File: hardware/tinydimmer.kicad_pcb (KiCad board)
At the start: 2 copper layers, 34 parts, among them J1 CTB7000/6, J2 CTB7000/2, Q1 IRL540N, SW1 SW_Push, T1 Hahn EL 305 2051, U1 BAJ0CC0T, U2 Digispark USB

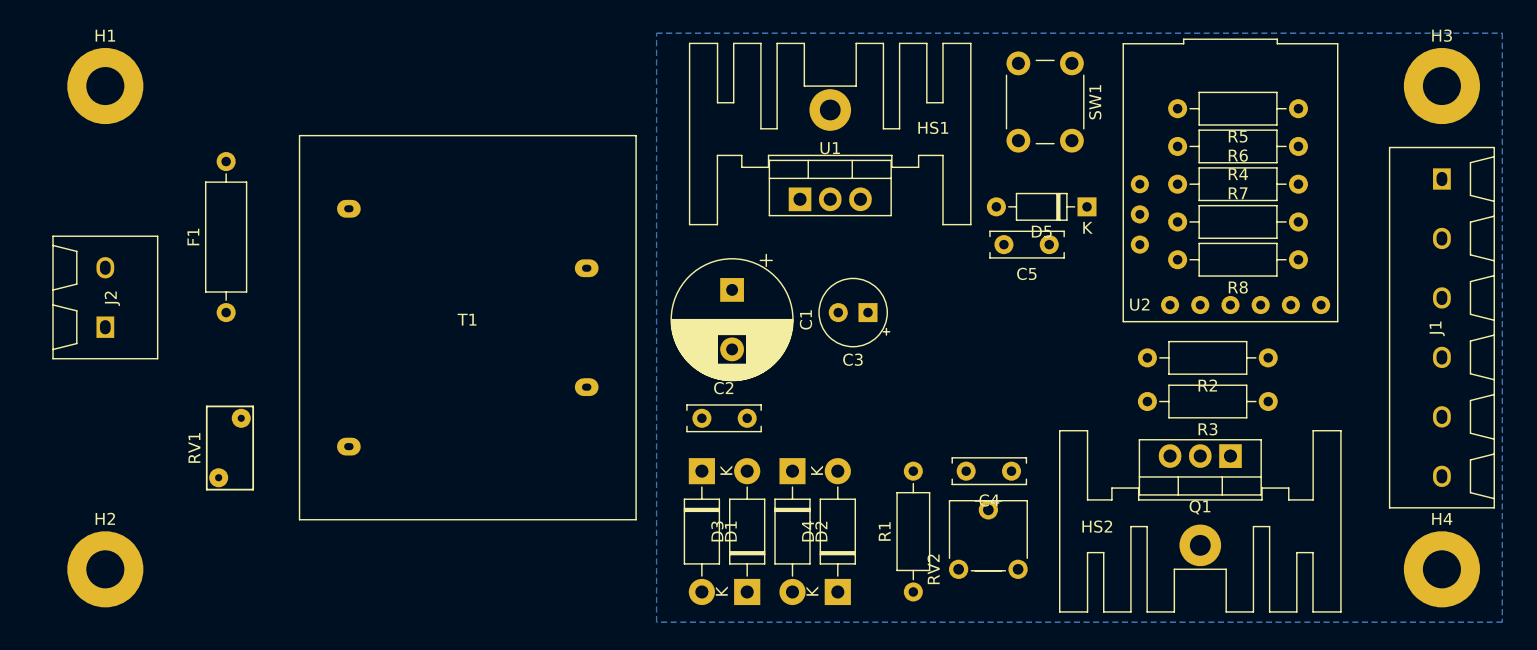
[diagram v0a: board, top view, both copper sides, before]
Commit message: Adjust pads, rewire connectors, change footprints
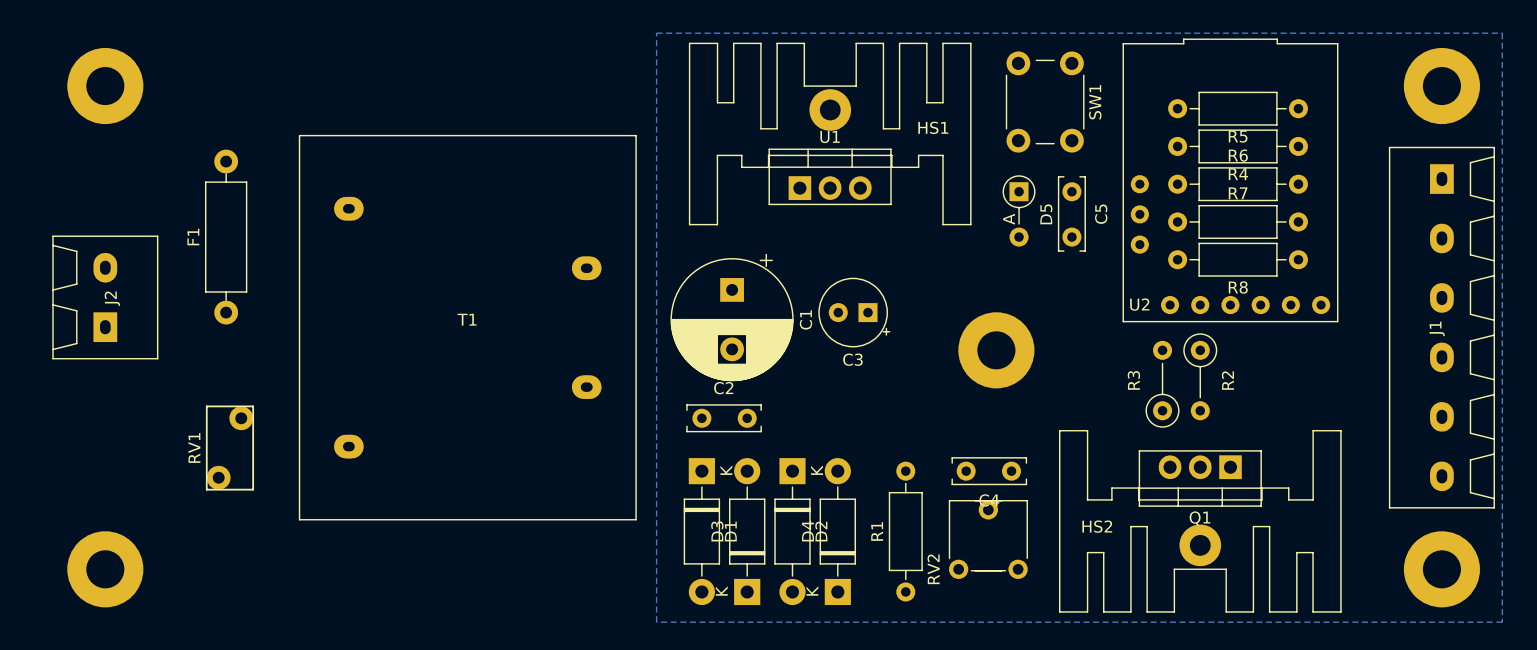
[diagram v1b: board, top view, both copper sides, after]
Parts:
- added H5: MountingHole_Pad, MountingHole:MountingHole_3.2mm_M3_Pad, F.Cu at (112.4, 65.4)
- D5: footprint Diode_THT:D_DO-35_SOD27_P7.62mm_Horizontal -> Diode_THT:D_DO-35_SOD27_P3.81mm_Vertical_AnodeUp
- R2, R3: footprint Resistor_THT:R_Axial_DIN0207_L6.3mm_D2.5mm_P10.16mm_Horizontal -> Resistor_THT:R_Axial_DIN0207_L6.3mm_D2.5mm_P5.08mm_Vertical
- moved R3 8.92 mm to (126.4, 70.5), turned to 90 degrees
- moved D5 5.85 mm to (114.3, 52.1), turned to 270 degrees
- moved R2 5.75 mm to (129.5, 65.4), turned to 270 degrees
- moved C5 5.24 mm to (118.7, 51.4), turned to 270 degrees
- moved U1 0.94 mm to (95.9, 51.8)
- moved Q1 0.94 mm to (132.1, 75.2)
- moved R1 0.63 mm to (104.8, 85.7)
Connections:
- J1 pad 1: SW_NEG -> SW_POS
- J1 pad 3: SW_POS -> GND
- J1 pad 5: GND -> SW_NEG
- R2 pad 1: Net-(Q1-Pad1) -> PWM
- R2 pad 2: PWM -> Net-(Q1-Pad1)

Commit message: First PCB draft
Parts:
- D5: footprint Diode_THT:D_DO-35_SOD27_P3.81mm_Vertical_AnodeUp -> Diode_THT:D_DO-35_SOD27_P7.62mm_Horizontal
- moved D5 17.1 mm to (128.3, 42.2), turned to 0 degrees
- moved C5 6.86 mm to (119.0, 58.3), turned to 180 degrees
- moved H3 1.00 mm to (148.9, 43.2)
- moved H4 1.00 mm to (148.9, 83.8)
- moved J1 1.00 mm to (148.9, 63.5)
- moved RV1 0.32 mm to (48.6, 71.1)
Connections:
- C5 pad 1: Net-(C5-Pad1) -> ENABLE
- D5 pad 1: Net-(C5-Pad1) -> Net-(D5-Pad1)
- R6 pad 1: Net-(C5-Pad1) -> Net-(D5-Pad1)
- R7 pad 2: Net-(C5-Pad1) -> Net-(D5-Pad1)
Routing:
- net POT_POS: track 0.00 -> 51.3 mm
- net +10V: track 0.00 -> 50.0 mm
- net Net-(D2-Pad2): track 0.00 -> 40.9 mm
- net Net-(C1-Pad1): track 0.00 -> 38.2 mm
- net SENSE: track 0.00 -> 31.2 mm
- net NEUT: track 0.00 -> 30.0 mm
- net Net-(R4-Pad1): track 0.00 -> 28.0 mm
- net Net-(D1-Pad2): track 0.00 -> 25.0 mm
- net Net-(F1-Pad1): track 0.00 -> 24.0 mm
- net Net-(D5-Pad1): track 0.00 -> 22.4 mm
- net RESET: track 0.00 -> 17.9 mm
- net ENABLE: track 0.00 -> 17.3 mm
- net LINE: track 0.00 -> 15.2 mm
- net SW_POS: track 0.00 -> 11.2 mm
- net Net-(Q1-Pad1): track 0.00 -> 9.64 mm
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- added copper zone on F.Cu, net SW_NEG
- added copper zone on B.Cu, net SW_POS
- added copper zone on F.Cu, net SW_POS
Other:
- board outline added: 125.2 x 50.2 mm
- net class Default: clearance 0.2 -> 0.25; trace_width 0.25 -> 0.5
- net class Mains added: clearance 1, trace_width 1.5, via_dia 0.8, via_drill 0.4
- net class Power added: clearance 0.5, trace_width 1.5, via_dia 0.8, via_drill 0.4
- rule trace_clearance: 0.2 -> 0.25
- board text added: "L"
- board text added: "LED+"
- board text added: "LED-"
- board text added: "N"
- board text added: "POT+"
- board text added: "POT-"
- board text added: "PSU+"
- board text added: "PSU-"

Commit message: Make labels more visible
Gerbers for first production batch
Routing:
- net SENSE: track 31.2 -> 31.8 mm
- net SW_POS: vias 0 -> 16
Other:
- board text added: "2A max"
- board text added: "RESET"

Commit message: Replace plain MOV with a protected GMOV
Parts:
- RV1: value 7N431K -> 14D271K; footprint Varistor:RV_Disc_D7mm_W3.9mm_P5mm -> Varistor:RV_Disc_D15.5mm_W3.9mm_P7.5mm
- moved F1 3.08 mm to (47.4, 59.2)
- moved RV1 1.31 mm to (48.4, 69.8)
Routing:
- net LINE: track 15.2 -> 17.6 mm
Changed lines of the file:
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@@
     (thickness 1.6)
     (drawings 18)
-    (tracks 108)
+    (tracks 104)
     (zones 0)
     (modules 35)
@@
     (add_net SW_NEG)
     (add_net SW_POS)
+  )
+  (module Varistor:RV_Disc_D15.5mm_W3.9mm_P7.5mm (layer F.Cu)
+    (at 48.4124 69.8246 270)
+    (descr "Varistor, diameter 15.5mm, width 3.9mm, pitch 7.5mm")
+    (tags "varistor SIOV")
+    (fp_text reference RV1 (at 3.75 3.65 90) (layer F.SilkS)
+      (effects (font (size 1 1) (thickness 0.15)))
+    )
+    (fp_text value 14D271K (at 3.75 -2.25 90) (layer F.Fab)
+      (effects (font (size 1 1) (thickness 0.15)))
+    )
+    (fp_line (start -4 -1.25) (end -4 2.65) (layer F.Fab) (width 0.1))
+    (fp_line (start 11.5 -1.25) (end 11.5 2.65) (layer F.Fab) (width 0.1))
+    (fp_line (start -4 -1.25) (end 11.5 -1.25) (layer F.Fab) (width 0.1))
+    (fp_line (start -4 2.65) (end 11.5 2.65) (layer F.Fab) (width 0.1))
+    (fp_line (start -4 -1.25) (end -4 2.65) (layer F.SilkS) (width 0.15))
+    (fp_line (start 11.5 -1.25) (end 11.5 2.65) (layer F.SilkS) (width 0.15))
+    (fp_line (start -4 -1.25) (end 11.5 -1.25) (layer F.SilkS) (width 0.15))
+    (fp_line (start -4 2.65) (end 11.5 2.65) (layer F.SilkS) (width 0.15))
+    (fp_line (start -4.25 -1.5) (end -4.25 2.9) (layer F.CrtYd) (width 0.05))
+    (fp_line (start 11.75 -1.5) (end 11.75 2.9) (layer F.CrtYd) (width 0.05))
+    (fp_line (start -4.25 -1.5) (end 11.75 -1.5) (layer F.CrtYd) (width 0.05))
+    (fp_line (start -4.25 2.9) (end 11.75 2.9) (layer F.CrtYd) (width 0.05))
+    (fp_text user %R (at 3.75 0.7 90) (layer F.Fab)
+      (effects (font (size 1 1) (thickness 0.15)))
+    )
+    (pad 2 thru_hole circle (at 7.5 1.4 270) (size 1.8 1.8) (drill 0.8) (layers *.Cu *.Mask)
+      (net 12 NEUT))
+    (pad 1 thru_hole circle (at 0 0 270) (size 1.8 1.8) (drill 0.8) (layers *.Cu *.Mask)
+      (net 7 "Net-(F1-Pad1)"))
+    (model ${KISYS3DMOD}/Varistor.3dshapes/RV_Disc_D15.5mm_W3.9mm_P7.5mm.wrl
+      (at (xyz 0 0 0))
+      (scale (xyz 1 1 1))
+      (rotate (xyz 0 0 0))
+    )
   )
   (module Diode_THT:D_DO-35_SOD27_P7.62mm_Horizontal (layer F.Cu)
@@
   )
   (module Resistor_THT:R_Axial_DIN0309_L9.0mm_D3.2mm_P12.70mm_Horizontal (layer F.Cu)
-    (at 47.625 62.23 90)
+    (at 47.3964 59.1566 90)
     (descr "Resistor, Axial_DIN0309 series, Axial, Horizontal, pin pitch=12.7mm, 0.5W = 1/2W, length*diameter=9*3.2mm^2, http://cdn-reichelt.de/documents/datenblatt/B400/1_4W%23YAG.pdf")
     (tags "Resistor Axial_DIN0309 series Axial Horizontal pin pitch 12.7mm 0.5W = 1/2W length 9mm diameter 3.2mm")
@@
     )
   )
-  (module Varistor:RV_Disc_D7mm_W3.9mm_P5mm (layer F.Cu)
-    (at 48.5775 71.12 270)
-    (descr "Varistor, diameter 7mm, width 3.9mm, pitch 5mm")
-    (tags "varistor SIOV")
-    (fp_text reference RV1 (at -2.3622 2.0447 180) (layer F.SilkS)
-      (effects (font (size 1 1) (thickness 0.15)))
-    )
-    (fp_text value 7N431K (at 2.5 -2 90) (layer F.Fab)
-      (effects (font (size 1 1) (thickness 0.15)))
-    )
-    (fp_text user %R (at 2.5 0.95 90) (layer F.Fab)
-      (effects (font (size 1 1) (thickness 0.15)))
-    )
-    (fp_line (start -1.25 3.15) (end 6.25 3.15) (layer F.CrtYd) (width 0.05))
-    (fp_line (start -1.25 -1.25) (end 6.25 -1.25) (layer F.CrtYd) (width 0.05))
-    (fp_line (start 6.25 -1.25) (end 6.25 3.15) (layer F.CrtYd) (width 0.05))
-    (fp_line (start -1.25 -1.25) (end -1.25 3.15) (layer F.CrtYd) (width 0.05))
-    (fp_line (start -1 2.9) (end 6 2.9) (layer F.SilkS) (width 0.15))
-    (fp_line (start -1 -1) (end 6 -1) (layer F.SilkS) (width 0.15))
-    (fp_line (start 6 -1) (end 6 2.9) (layer F.SilkS) (width 0.15))
-    (fp_line (start -1 -1) (end -1 2.9) (layer F.SilkS) (width 0.15))
-    (fp_line (start -1 2.9) (end 6 2.9) (layer F.Fab) (width 0.1))
-    (fp_line (start -1 -1) (end 6 -1) (layer F.Fab) (width 0.1))
-    (fp_line (start 6 -1) (end 6 2.9) (layer F.Fab) (width 0.1))
-    (fp_line (start -1 -1) (end -1 2.9) (layer F.Fab) (width 0.1))
-    (pad 1 thru_hole circle (at 0 0 270) (size 2 2) (drill 0.8) (layers *.Cu *.Mask)
-      (net 7 "Net-(F1-Pad1)"))
-    (pad 2 thru_hole circle (at 5 1.9 270) (size 2 2) (drill 0.8) (layers *.Cu *.Mask)
-      (net 12 NEUT))
-    (model ${KISYS3DMOD}/Varistor.3dshapes/RV_Disc_D7mm_W3.9mm_P5mm.wrl
-      (at (xyz 0 0 0))
-      (scale (xyz 1 1 1))
-      (rotate (xyz 0 0 0))
-    )
-  )
   (module custom-parts:Potentiometer_ACP_CA6-V2,5_Vertical (layer F.Cu)
     (at 109.22 83.82 90)
@@
       (net 3 +10V))
   )
-  (gr_text "2A max" (at 44.704 55.88 90) (layer F.SilkS)
+  (gr_text "2A max" (at 44.5389 52.8701 90) (layer F.SilkS)
     (effects (font (size 1 1) (thickness 0.15)))
   )
@@
   (segment (start 82.55 75.946) (end 88.138 81.534) (width 1.5) (layer F.Cu) (net 6))
   (segment (start 92.614634 81.534) (end 95.25 84.169366) (width 1.5) (layer F.Cu) (net 6))
-  (segment (start 56.355 53.5) (end 57.945 53.5) (width 1.5) (layer B.Cu) (net 7))
-  (segment (start 47.625 62.23) (end 56.355 53.5) (width 1.5) (layer B.Cu) (net 7))
-  (segment (start 48.624999 63.229999) (end 47.625 62.23) (width 1.5) (layer B.Cu) (net 7))
-  (segment (start 49.577499 64.182499) (end 48.624999 63.229999) (width 1.5) (layer B.Cu) (net 7))
-  (segment (start 49.577499 70.120001) (end 49.577499 64.182499) (width 1.5) (layer B.Cu) (net 7))
-  (segment (start 48.5775 71.12) (end 49.577499 70.120001) (width 1.5) (layer B.Cu) (net 7))
-  (segment (start 44.145 49.53) (end 46.210787 49.53) (width 1.5) (layer B.Cu) (net 8))
-  (segment (start 46.210787 49.53) (end 47.625 49.53) (width 1.5) (layer B.Cu) (net 8))
-  (segment (start 37.465 56.21) (end 44.145 49.53) (width 1.5) (layer B.Cu) (net 8))
-  (segment (start 37.465 58.46) (end 37.465 56.21) (width 1.5) (layer B.Cu) (net 8))
+  (segment (start 53.053 53.5) (end 47.3964 59.1566) (width 1.5) (layer B.Cu) (net 7))
+  (segment (start 57.945 53.5) (end 53.053 53.5) (width 1.5) (layer B.Cu) (net 7))
+  (segment (start 47.3964 68.8086) (end 48.4124 69.8246) (width 1.5) (layer B.Cu) (net 7))
+  (segment (start 47.3964 59.1566) (end 47.3964 68.8086) (width 1.5) (layer B.Cu) (net 7))
+  (segment (start 37.465 58.46) (end 37.465 53.848) (width 1.5) (layer B.Cu) (net 8))
+  (segment (start 44.8564 46.4566) (end 47.3964 46.4566) (width 1.5) (layer B.Cu) (net 8))
+  (segment (start 37.465 53.848) (end 44.8564 46.4566) (width 1.5) (layer B.Cu) (net 8))
   (segment (start 129.54 75.2348) (end 129.54 81.805) (width 1.5) (layer F.Cu) (net 9))
   (via (at 146.812 48.768) (size 0.8) (drill 0.4) (layers F.Cu B.Cu) (net 10))
@@
   (segment (start 146.504 76) (end 148.86 76) (width 0.5) (layer B.Cu) (net 11))
   (segment (start 111.76 86.36) (end 137.922 86.36) (width 0.5) (layer B.Cu) (net 11))
-  (segment (start 57.945 75.5) (end 57.945 73.5) (width 1.5) (layer B.Cu) (net 12))
-  (segment (start 57.325 76.12) (end 57.945 75.5) (width 1.5) (layer B.Cu) (net 12))
-  (segment (start 46.6775 76.12) (end 57.325 76.12) (width 1.5) (layer B.Cu) (net 12))
-  (segment (start 37.465 66.9075) (end 37.465 63.46) (width 1.5) (layer B.Cu) (net 12))
-  (segment (start 46.6775 76.12) (end 37.465 66.9075) (width 1.5) (layer B.Cu) (net 12))
+  (segment (start 37.465 67.7772) (end 47.0124 77.3246) (width 1.5) (layer B.Cu) (net 12))
+  (segment (start 37.465 63.46) (end 37.465 67.7772) (width 1.5) (layer B.Cu) (net 12))
+  (segment (start 54.1204 77.3246) (end 57.945 73.5) (width 1.5) (layer B.Cu) (net 12))
+  (segment (start 47.0124 77.3246) (end 54.1204 77.3246) (width 1.5) (layer B.Cu) (net 12))
   (segment (start 126.365 70.485) (end 129.54 70.485) (width 0.5) (layer F.Cu) (net 13))
   (segment (start 132.08 73.7348) (end 132.08 75.2348) (width 0.5) (layer F.Cu) (net 13))

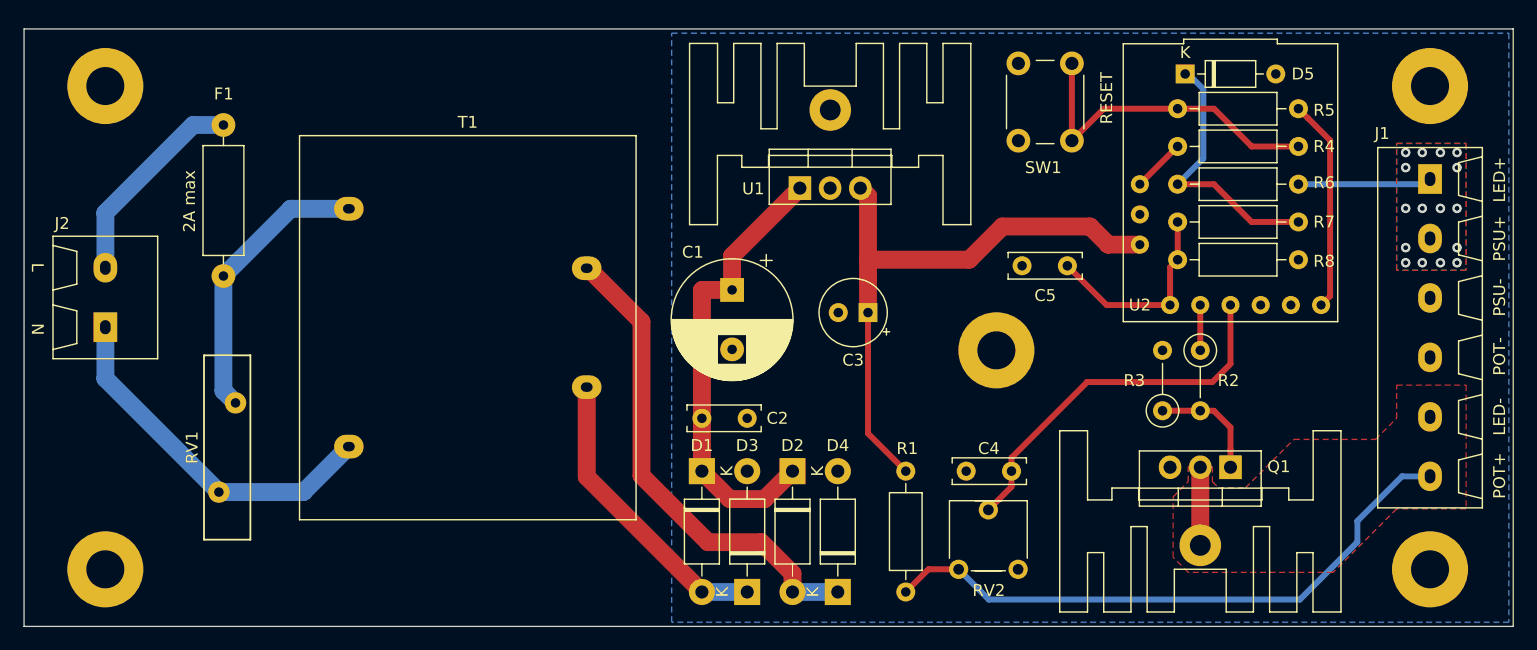
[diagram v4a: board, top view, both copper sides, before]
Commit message: Migrate to KiCad 6
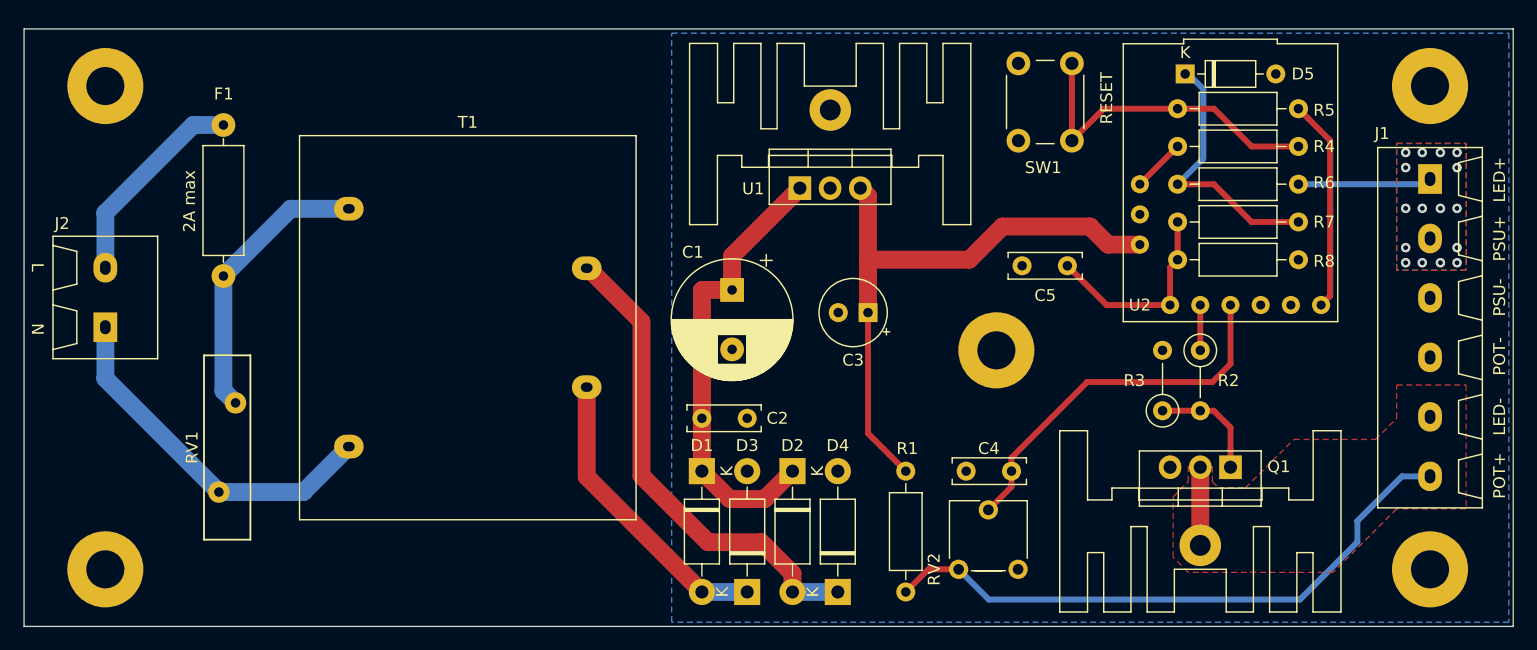
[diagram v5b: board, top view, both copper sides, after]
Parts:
- F1: footprint Resistor_THT:R_Axial_DIN0309_L9.0mm_D3.2mm_P12.70mm_Horizontal -> custom-parts:R_Axial_DIN0309_L9.0mm_D3.2mm_P12.70mm_Horizontal_Large_Pads
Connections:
- H1 pad 1: Net-(H1-Pad1) -> unconnected-(H1-Pad1)
- H2 pad 1: Net-(H2-Pad1) -> unconnected-(H2-Pad1)
- U2 pad 4: Net-(U2-Pad4) -> unconnected-(U2-Pad4)
- U2 pad 5: Net-(U2-Pad5) -> unconnected-(U2-Pad5)
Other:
- net class Default removed
- net class Mains removed
- net class Power removed
